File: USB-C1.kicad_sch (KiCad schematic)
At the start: 32 parts, among them J2 USB_C_Receptacle, J3 I2C_HD3SS3220, U3 HD3SS3220IRNHR, U4 TPS2068EDBVR, U5 TPD4E02B04DQA, U6 TPD4E02B04DQA, U7 TPD4E02B04DQA

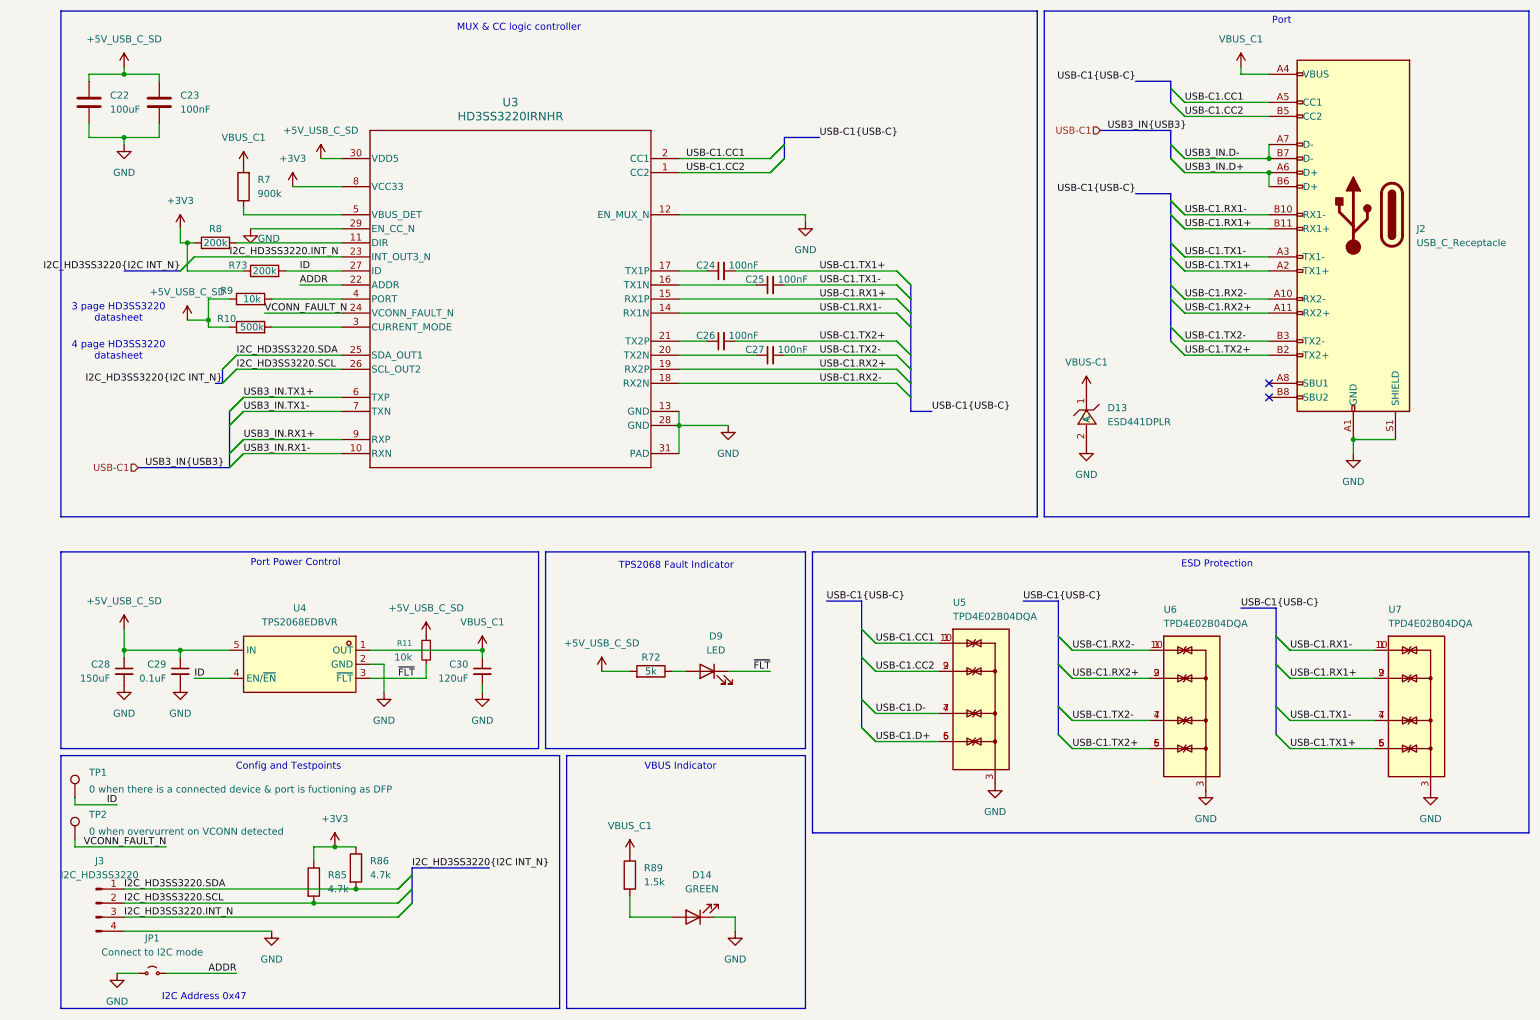
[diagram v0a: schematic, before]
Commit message: Schematic reannotated
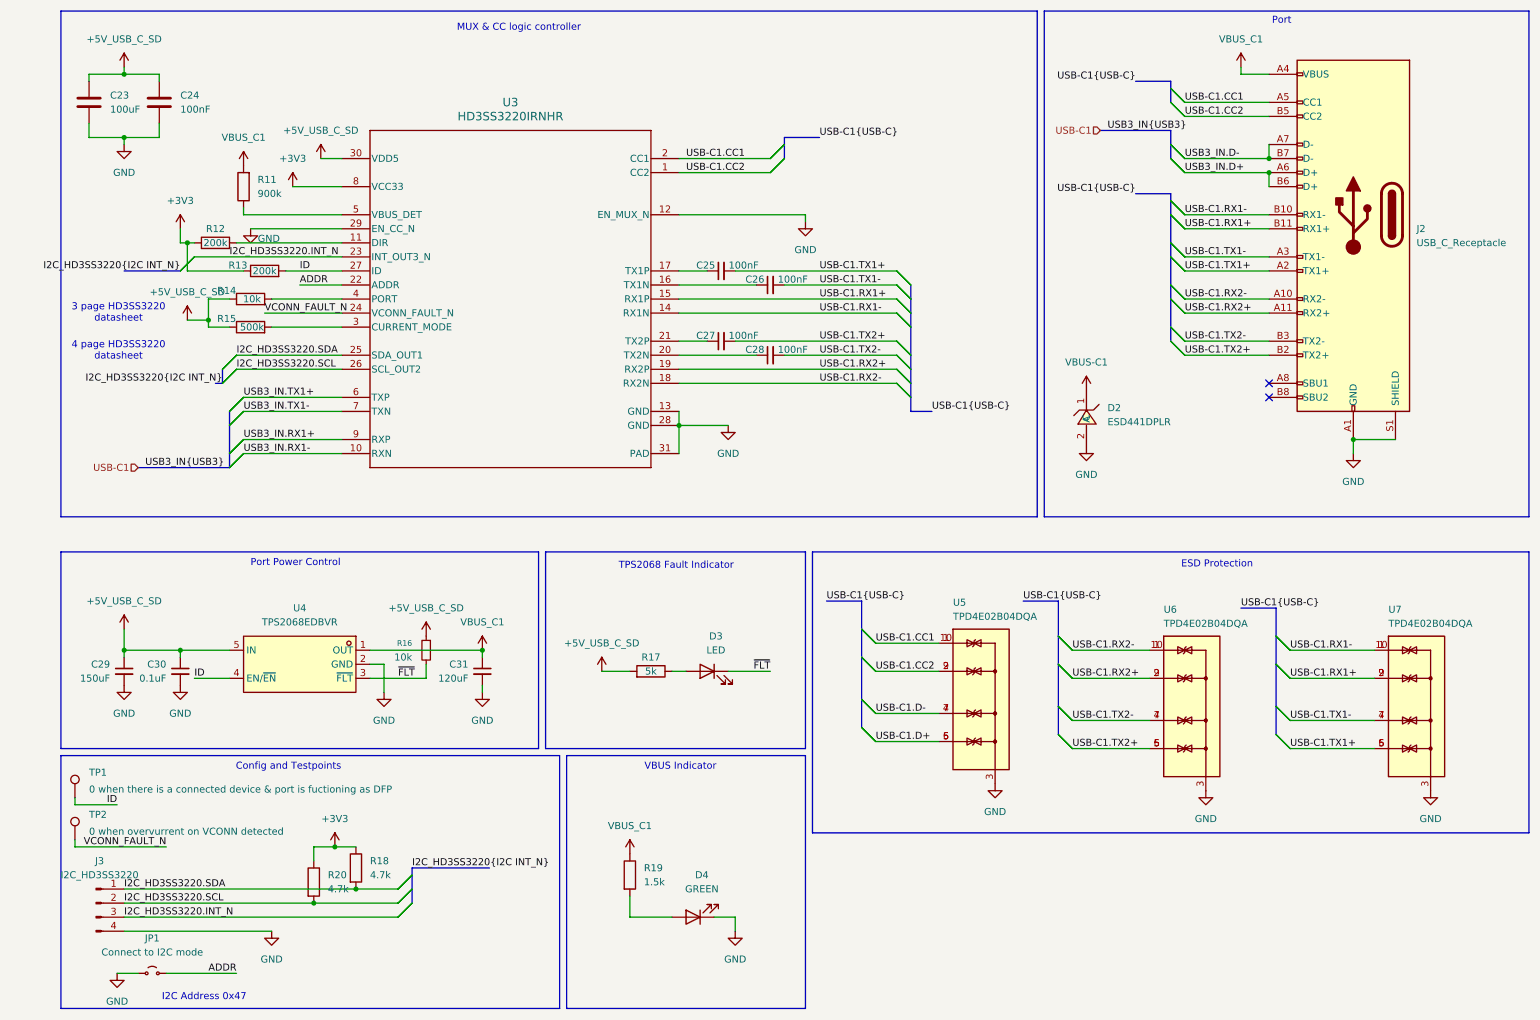
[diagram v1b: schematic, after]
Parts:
- renumbered C22 to C23, C23 to C24, C24 to C25, C25 to C26, C26 to C27, C27 to C28, C28 to C29, C29 to C30, C30 to C31, D13 to D2, D9 to D3, D14 to D4, R7 to R11, R8 to R12, R73 to R13, R9 to R14, R10 to R15, R11 to R16, R72 to R17, R86 to R18, R89 to R19, R85 to R20

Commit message: J11 changed to 8-pin PCIe connector, footprint assigned
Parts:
- D3, D4: footprint (none) -> LED_SMD:LED_0603_1608Metric
- J2: footprint Connector_USB:USB_C_Receptacle_Amphenol_12401610E4-2A -> SamacSys_Parts:USB420003A
- R13, R17, R18, R19, R20: footprint (none) -> Resistor_SMD:R_0402_1005Metric
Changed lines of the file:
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@@
 			)
 		)
-		(property "Footprint" ""
+		(property "Footprint" "Resistor_SMD:R_0402_1005Metric"
 			(at 66.802 168.91 90)
 			(effects
@@
 			)
 		)
-		(property "Footprint" ""
+		(property "Footprint" "LED_SMD:LED_0603_1608Metric"
 			(at 129.54 177.8 0)
 			(effects
@@
 			)
 		)
-		(property "Footprint" ""
+		(property "Footprint" "LED_SMD:LED_0603_1608Metric"
 			(at 132.08 133.35 0)
 			(effects
@@
 			)
 		)
-		(property "Footprint" ""
+		(property "Footprint" "Resistor_SMD:R_0402_1005Metric"
 			(at 116.332 170.18 90)
 			(effects
@@
 			)
 		)
-		(property "Footprint" ""
+		(property "Footprint" "Resistor_SMD:R_0402_1005Metric"
 			(at 59.182 171.45 90)
 			(effects
@@
 			)
 		)
-		(property "Footprint" ""
+		(property "Footprint" "Resistor_SMD:R_0402_1005Metric"
 			(at 121.92 135.128 90)
 			(effects
@@
 			)
 		)
-		(property "Footprint" "Connector_USB:USB_C_Receptacle_Amphenol_12401610E4-2A"
+		(property "Footprint" "SamacSys_Parts:USB420003A"
 			(at 245.11 50.8 0)
 			(effects
@@
 			)
 		)
-		(property "Footprint" ""
+		(property "Footprint" "Resistor_SMD:R_0402_1005Metric"
 			(at 52.07 62.738 90)
 			(effects

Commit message: footprints assigned, U21 change to SiRA80DP
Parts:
- TP1, TP2: footprint TestPoint:TestPoint_2Pads_Pitch5.08mm_Drill1.3mm -> TestPoint:TestPoint_Loop_D1.80mm_Drill1.0mm_Beaded
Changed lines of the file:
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@@
 			)
 		)
-		(property "Footprint" "TestPoint:TestPoint_2Pads_Pitch5.08mm_Drill1.3mm"
+		(property "Footprint" "TestPoint:TestPoint_Loop_D1.80mm_Drill1.0mm_Beaded"
 			(at 22.86 163.83 0)
 			(effects
@@
 			)
 		)
-		(property "Footprint" "TestPoint:TestPoint_2Pads_Pitch5.08mm_Drill1.3mm"
+		(property "Footprint" "TestPoint:TestPoint_Loop_D1.80mm_Drill1.0mm_Beaded"
 			(at 22.86 156.21 0)
 			(effects

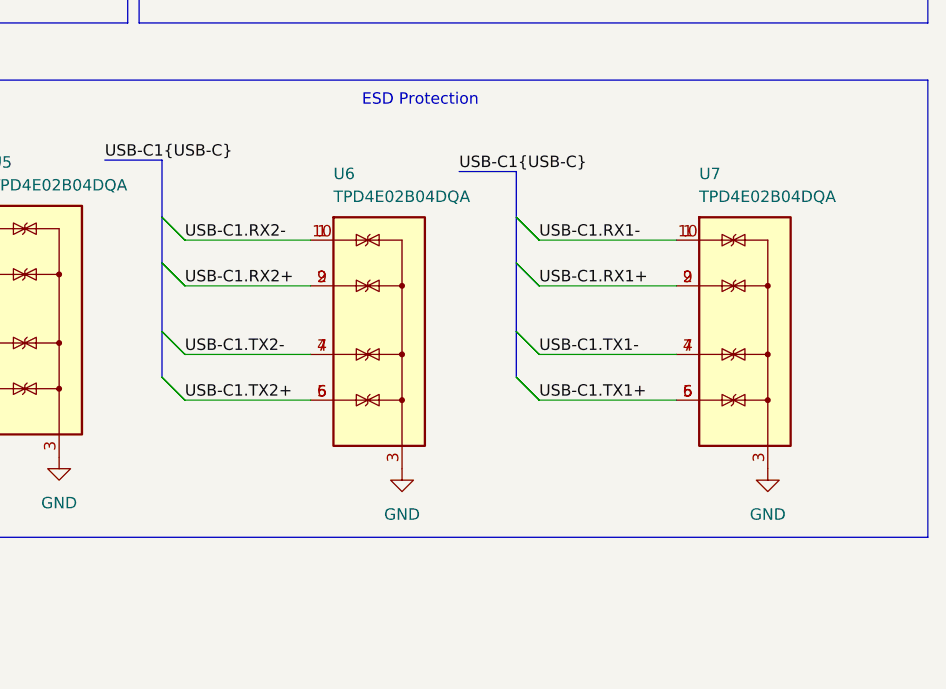
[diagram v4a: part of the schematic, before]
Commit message: Next net class label fixes, swap of the SS lines for better routing
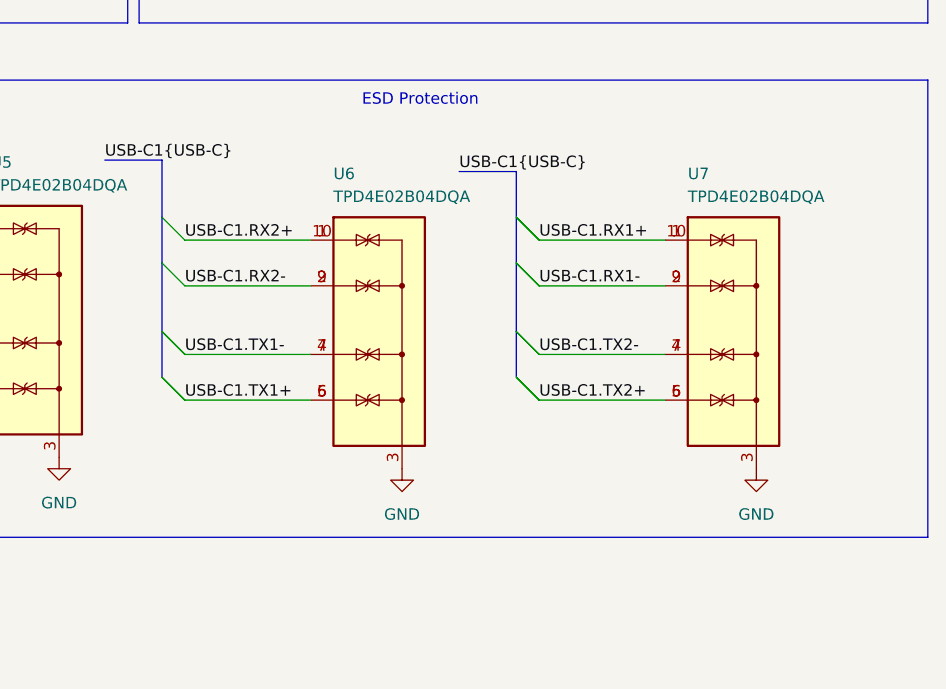
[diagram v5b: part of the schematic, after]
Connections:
- net USB-C1.RX1+: now also U7.1 (IO1), U7.10 (NC); no longer U7.2 (IO2), U7.9 (NC)
- net USB-C1.RX1-: now also U7.2 (IO2), U7.9 (NC); no longer U7.1 (IO1), U7.10 (NC)
- net USB-C1.RX2+: now also U6.1 (IO1), U6.10 (NC); no longer U6.2 (IO2), U6.9 (NC)
- net USB-C1.RX2-: now also U6.2 (IO2), U6.9 (NC); no longer U6.1 (IO1), U6.10 (NC)
- net USB-C1.TX1+: now also U6.5 (IO4), U6.6 (NC); no longer U7.5 (IO4), U7.6 (NC)
- net USB-C1.TX1-: now also U6.4 (IO3), U6.7 (NC); no longer U7.4 (IO3), U7.7 (NC)
- net USB-C1.TX2+: now also U7.5 (IO4), U7.6 (NC); no longer U6.5 (IO4), U6.6 (NC)
- net USB-C1.TX2-: now also U7.4 (IO3), U7.7 (NC); no longer U6.4 (IO3), U6.7 (NC)
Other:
- moved on the sheet: U7

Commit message: Added lcsc part number for most of components, fixes for better routing
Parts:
- C23: footprint Capacitor_THT:C_Radial_D10.0mm_H16.0mm_P5.00mm -> Capacitor_THT:C_Radial_D6.3mm_H11.0mm_P2.50mm; LCSC Part (none) -> C109392
- C24, C25, C26, C27, C28, C30: LCSC Part (none) -> C5182432
- C29: footprint Capacitor_THT:C_Radial_D10.0mm_H16.0mm_P5.00mm -> Capacitor_THT:C_Radial_D6.3mm_H11.0mm_P2.50mm; LCSC Part (none) -> C338186
- C31: footprint Capacitor_THT:C_Radial_D10.0mm_H16.0mm_P5.00mm -> Capacitor_THT:C_Radial_D6.3mm_H11.0mm_P2.50mm; LCSC Part (none) -> C442816
- D3: value LED -> RED; LCSC Part (none) -> C497918
- D4: LCSC Part (none) -> C22371298
- U3: LCSC Part (none) -> C165155
- U5, U6, U7: LCSC Part (none) -> C106794
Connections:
- net VBUS-C1 is gone; now on net VBUS_C1: D2.1 (C)
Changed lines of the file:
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@@
 			)
 		)
+		(property "LCSC Part" "C22371298"
+			(at 129.54 177.8 0)
+			(effects
+				(font
+					(size 1.27 1.27)
+				)
+				(hide yes)
+			)
+		)
 		(pin "1"
 		)
@@
 			)
 		)
+		(property "LCSC Part" "C5182432"
+			(at 134.62 60.96 90)
+			(effects
+				(font
+					(size 1.27 1.27)
+				)
+				(hide yes)
+			)
+		)
 		(pin "2"
 		)
@@
 			)
 		)
-		(property "Value" "LED"
+		(property "Value" "RED"
 			(at 133.6675 129.54 0)
 			(effects
@@
 			)
 		)
+		(property "LCSC Part" "C497918"
+			(at 132.08 133.35 0)
+			(effects
+				(font
+					(size 1.27 1.27)
+				)
+				(hide yes)
+			)
+		)
 		(pin "2"
 		)
@@
 			)
 		)
+		(property "LCSC Part" "C5182432"
+			(at 143.51 63.5 90)
+			(effects
+				(font
+					(size 1.27 1.27)
+				)
+				(hide yes)
+			)
+		)
 		(pin "2"
 		)
@@
 			)
 		)
-		(property "Footprint" "Capacitor_THT:C_Radial_D10.0mm_H16.0mm_P5.00mm"
+		(property "Footprint" "Capacitor_THT:C_Radial_D6.3mm_H11.0mm_P2.50mm"
 			(at 26.67 133.35 0)
 			(effects
@@
 			)
 		)
+		(property "LCSC Part" "C338186"
+			(at 26.67 133.35 0)
+			(effects
+				(font
+					(size 1.27 1.27)
+				)
+				(hide yes)
+			)
+		)
 		(pin "1"
 		)
@@
 			)
 		)
+		(property "LCSC Part" "C5182432"
+			(at 36.83 133.35 0)
+			(effects
+				(font
+					(size 1.27 1.27)
+				)
+				(hide yes)
+			)
+		)
 		(pin "1"
 		)
@@
 			)
 		)
+		(property "LCSC Part" "C106794"
+			(at 219.71 139.7 0)
+			(effects
+				(font
+					(size 1.27 1.27)
+				)
+				(hide yes)
+			)
+		)
 		(pin "5"
 		)
@@
 			)
 		)
+		(property "LCSC Part" "C106794"
+			(at 181.61 138.43 0)
+			(effects
+				(font
+					(size 1.27 1.27)
+				)
+				(hide yes)
+			)
+		)
 		(pin "5"
 		)
@@
 			)
 		)
+		(property "LCSC Part" "C5182432"
+			(at 143.51 76.2 90)
+			(effects
+				(font
+					(size 1.27 1.27)
+				)
+				(hide yes)
+			)
+		)
 		(pin "2"
 		)
@@
 			)
 		)
-		(property "Footprint" "Capacitor_THT:C_Radial_D10.0mm_H16.0mm_P5.00mm"
+		(property "Footprint" "Capacitor_THT:C_Radial_D6.3mm_H11.0mm_P2.50mm"
 			(at 21.2852 34.29 0)
 			(effects
@@
 			)
 		)
+		(property "LCSC Part" "C109392"
+			(at 20.32 30.48 0)
+			(effects
+				(font
+					(size 1.27 1.27)
+				)
+				(hide yes)
+			)
+		)
 		(pin "2"
 		)
@@
 			)
 		)
+		(property "LCSC Part" "C5182432"
+			(at 33.02 30.48 0)
+			(effects
+				(font
+					(size 1.27 1.27)
+				)
+				(hide yes)
+			)
+		)
 		(pin "2"
 		)
@@
 			)
 		)
-		(property "Footprint" "Capacitor_THT:C_Radial_D10.0mm_H16.0mm_P5.00mm"
+		(property "Footprint" "Capacitor_THT:C_Radial_D6.3mm_H11.0mm_P2.50mm"
 			(at 91.44 133.35 0)
 			(effects
@@
 			)
 		)
+		(property "LCSC Part" "C442816"
+			(at 91.44 133.35 0)
+			(effects
+				(font
+					(size 1.27 1.27)
+				)
+				(hide yes)
+			)
+		)
 		(pin "1"
 		)
@@
 	)
 	(symbol
+		(lib_id "power:VBUS")
+		(at 200.66 82.55 0)
+		(unit 1)
+		(exclude_from_sim no)
+		(in_bom yes)
+		(on_board yes)
+		(dnp no)
+		(fields_autoplaced yes)
+		(property "Reference" "#PWR032"
+			(at 200.66 86.36 0)
+			(effects
+				(font
+					(size 1.27 1.27)
+				)
+				(hide yes)
+			)
+		)
+		(property "Value" "VBUS_C1"
+			(at 200.66 77.47 0)
+			(effects
+				(font
+					(size 1.27 1.27)
+				)
+			)
+		)
+		(property "Footprint" ""
+			(at 200.66 82.55 0)
+			(effects
+				(font
+					(size 1.27 1.27)
+				)
+				(hide yes)
+			)
+		)
+		(property "Datasheet" ""
+			(at 200.66 82.55 0)
+			(effects
+				(font
+					(size 1.27 1.27)
+				)
+				(hide yes)
+			)
+		)
+		(property "Description" "Power symbol creates a global label with name \"VBUS\""
+			(at 200.66 82.55 0)
+			(effects
+				(font
+					(size 1.27 1.27)
+				)
+				(hide yes)
+			)
+		)
+		(pin "1"
+		)
+		(instances
+			(project "USB_hub"
+				(path "/a2586c28-95f1-49e6-9254-37d7a8473e53/9818f2bb-7888-47ed-88c0-ae123f59f09a"
+					(reference "#PWR032")
+					(unit 1)
+				)
+			)
+		)
+	)
+	(symbol
 		(lib_id "2025-07-15_13-22-11:HD3SS3220IRNHR")
 		(at 96.52 66.04 0)
@@
 			)
 		)
+		(property "LCSC Part" "C165155"
+			(at 96.52 66.04 0)
+			(effects
+				(font
+					(size 1.27 1.27)
+				)
+				(hide yes)
+			)
+		)
 		(pin "29"
 		)
@@
 			)
 		)
+		(property "LCSC Part" "C5182432"
+			(at 134.62 73.66 90)
+			(effects
+				(font
+					(size 1.27 1.27)
+				)
+				(hide yes)
+			)
+		)
 		(pin "2"
 		)
@@
 	)
 	(symbol
-		(lib_id "power:VBUS")
-		(at 200.66 82.55 0)
-		(unit 1)
-		(exclude_from_sim no)
-		(in_bom yes)
-		(on_board yes)
-		(dnp no)
-		(fields_autoplaced yes)
-		(property "Reference" "#PWR032"
-			(at 200.66 86.36 0)
-			(effects
-				(font
-					(size 1.27 1.27)
-				)
-				(hide yes)
-			)
-		)
-		(property "Value" "VBUS-C1"
-			(at 200.66 77.47 0)
-			(effects
-				(font
-					(size 1.27 1.27)
-				)
-			)
-		)
-		(property "Footprint" ""
-			(at 200.66 82.55 0)
-			(effects
-				(font
-					(size 1.27 1.27)
-				)
-				(hide yes)
-			)
-		)
-		(property "Datasheet" ""
-			(at 200.66 82.55 0)
-			(effects
-				(font
-					(size 1.27 1.27)
-				)
-				(hide yes)
-			)
-		)
-		(property "Description" "Power symbol creates a global label with name \"VBUS\""
-			(at 200.66 82.55 0)
-			(effects
-				(font
-					(size 1.27 1.27)
-				)
-				(hide yes)
-			)
-		)
-		(pin "1"
-		)
-		(instances
-			(project "USB_hub"
-				(path "/a2586c28-95f1-49e6-9254-37d7a8473e53/9818f2bb-7888-47ed-88c0-ae123f59f09a"
-					(reference "#PWR032")
-					(unit 1)
-				)
-			)
-		)
-	)
-	(symbol
 		(lib_id "power:GND")
 		(at 91.44 137.16 0)
@@
 			(at 259.08 139.7 0)
 			(effects
+				(font
+					(size 1.27 1.27)
+				)
+				(hide yes)
+			)
+		)
+		(property "LCSC Part" "C106794"
+			(at 259.08 139.7 0)
+			(effects

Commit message: Added lcsc part number for most of resistors
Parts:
- R12, R13: LCSC Part (none) -> C25764
- R14, R16: LCSC Part (none) -> C25744
- R15: footprint Resistor_SMD:R_0402_1005Metric -> Resistor_SMD:R_0603_1608Metric; LCSC Part (none) -> C2902631
- R17: LCSC Part (none) -> C5948099
- R18, R20: LCSC Part (none) -> C105871
- R19: LCSC Part (none) -> C327253
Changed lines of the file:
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@@
 			)
 		)
+		(property "LCSC Part" "C105871"
+			(at 68.58 168.91 0)
+			(effects
+				(font
+					(size 1.27 1.27)
+				)
+				(hide yes)
+			)
+		)
 		(pin "2"
 		)
@@
 			)
 		)
+		(property "LCSC Part" "C25764 "
+			(at 43.18 55.88 90)
+			(effects
+				(font
+					(size 1.27 1.27)
+				)
+				(hide yes)
+			)
+		)
 		(pin "1"
 		)
@@
 			)
 		)
+		(property "LCSC Part" "C327253 "
+			(at 118.11 170.18 0)
+			(effects
+				(font
+					(size 1.27 1.27)
+				)
+				(hide yes)
+			)
+		)
 		(pin "2"
 		)
@@
 			)
 		)
+		(property "LCSC Part" "C105871"
+			(at 60.96 171.45 0)
+			(effects
+				(font
+					(size 1.27 1.27)
+				)
+				(hide yes)
+			)
+		)
 		(pin "2"
 		)
@@
 			)
 		)
-		(property "Footprint" "Resistor_SMD:R_0402_1005Metric"
+		(property "Footprint" "Resistor_SMD:R_0603_1608Metric"
 			(at 49.53 72.898 90)
 			(effects
@@
 			)
 		)
+		(property "LCSC Part" "C2902631 "
+			(at 49.53 71.12 90)
+			(effects
+				(font
+					(size 1.27 1.27)
+				)
+				(hide yes)
+			)
+		)
 		(pin "2"
 		)
@@
 			)
 		)
+		(property "LCSC Part" "C5948099 "
+			(at 121.92 133.35 90)
+			(effects
+				(font
+					(size 1.27 1.27)
+				)
+				(hide yes)
+			)
+		)
 		(pin "1"
 		)
@@
 			)
 		)
+		(property "LCSC Part" "C25744"
+			(at 81.28 129.54 0)
+			(effects
+				(font
+					(size 1.27 1.27)
+				)
+				(hide yes)
+			)
+		)
 		(pin "2"
 		)
@@
 			)
 		)
+		(property "LCSC Part" "C25744"
+			(at 49.53 66.04 90)
+			(effects
+				(font
+					(size 1.27 1.27)
+				)
+				(hide yes)
+			)
+		)
 		(pin "2"
 		)
@@
 			(effects
 				(font
+					(size 1.27 1.27)
+				)
+				(hide yes)
+			)
+		)
+		(property "LCSC Part" "C25764 "
+			(at 52.07 60.96 90)
+			(effects
+				(font
